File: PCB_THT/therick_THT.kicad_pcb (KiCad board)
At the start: 2 copper layers, 227 x 76.9 mm, 107 parts, among them J1 TYPE-C-31-M12_13, J2 4PIN, K1 KEYSW, K10 KEYSW, K11 KEYSW, K12 KEYSW, K13 KEYSW, K14 KEYSW, K15 KEYSW, K16 KEYSW, K17 KEYSW, K18 KEYSW, K19 KEYSW, K2 KEYSW, K20 KEYSW, K21 KEYSW, K22 KEYSW, K23 KEYSW, K24 KEYSW, K25 KEYSW, K26 KEYSW, K27 KEYSW, K28 KEYSW, K29 KEYSW, K3 KEYSW, K30 KEYSW, K31 KEYSW, K32 KEYSW, K33 KEYSW, K34 KEYSW, K35 KEYSW, K36 KEYSW, K37 KEYSW, K38 KEYSW, K39 KEYSW, K4 KEYSW, K40 KEYSW, K41 KEYSW, K42 KEYSW, K43 KEYSW, K44 KEYSW, K45 KEYSW, K46 KEYSW, K47 KEYSW, K48 KEYSW, K5 KEYSW, K6 KEYSW, K7 KEYSW, K8 KEYSW, K9 KEYSW, SW1 SW_PUSH, U1 ProMicro, U2 HOLE

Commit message: Slimmed down USB port
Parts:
- J1: footprint acheron_Connectors:TYPE-C-31-M-12 -> random-keyboard-parts:TYPE-C-31-M-12
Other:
- board size 227 x 76.9 mm -> 227 x 76.7 mm
- board text removed: "TYPE-C-31-M12"
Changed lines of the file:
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@@
   (general
     (thickness 1.6)
-    (drawings 36)
+    (drawings 35)
     (tracks 289)
     (zones 0)
@@
     (38 B.Mask user)
     (39 F.Mask user)
-    (40 Dwgs.User user)
+    (40 Dwgs.User user hide)
     (41 Cmts.User user)
     (42 Eco1.User user)
@@
     (46 B.CrtYd user)
     (47 F.CrtYd user)
-    (48 B.Fab user)
+    (48 B.Fab user hide)
     (49 F.Fab user)
   )
@@
     (uvia_min_size 0.2)
     (uvia_min_drill 0.1)
-    (edge_width 0.15)
+    (edge_width 0.05)
     (segment_width 0.15)
     (pcb_text_width 0.3)
@@
     (aux_axis_origin 160.3375 73.025)
     (grid_origin 160.3375 73.025)
-    (visible_elements 7FFFEFFF)
+    (visible_elements 7FFFFFFF)
     (pcbplotparams
       (layerselection 0x010fc_ffffffff)
@@
       (drillshape 0)
       (scaleselection 1)
-      (outputdirectory "../Gerber/"))
+      (outputdirectory "Gerber/"))
   )
   (net 0 "")
@@
     (uvia_drill 0.2)
   )
-  (module acheron_Connectors:TYPE-C-31-M-12 (layer B.Cu)
+  (module random-keyboard-parts:TYPE-C-31-M-12 (layer B.Cu)
     (at 84.1375 40.408625)
-    (fp_text reference J1 (at 0 -5) (layer B.SilkS)
-      (effects (font (size 1 1) (thickness 0.15)) (justify mirror))
+    (fp_text reference J1 (at -0.0127 -2.7305 180) (layer Dwgs.User)
+      (effects (font (size 1 1) (thickness 0.15)))
     )
-    (fp_text value TYPE-C-31-M12_13 (at 0.05 -7.35) (layer B.Fab)
+    (fp_text value TYPE-C-31-M12_13 (at 0.05 -7.35 180) (layer B.Fab)
       (effects (font (size 0.5 0.5) (thickness 0.125)) (justify mirror))
     )
-    (fp_line (start 4.8 -8.42) (end -4.8 -8.42) (layer Cmts.User) (width 0.15))
-    (fp_text user "KEEPOUT ZONE" (at 0 -4) (layer B.Fab)
+    (fp_line (start 5 -1.4) (end -5 -1.4) (layer Dwgs.User) (width 0.12))
+    (fp_line (start 5 -6.8) (end 5 -1.4) (layer Dwgs.User) (width 0.12))
+    (fp_line (start -5 -6.8) (end 5 -6.8) (layer Dwgs.User) (width 0.12))
+    (fp_line (start -5 -1.4) (end -5 -6.8) (layer Dwgs.User) (width 0.12))
+    (fp_text user "USB Connector" (at -0.0254 -4.7498) (layer B.SilkS)
+      (effects (font (size 0.5 0.5) (thickness 0.125)) (justify mirror))
+    )
+    (fp_text user TYPE-C-M-12 (at -0.0127 -4.0132) (layer B.SilkS)
       (effects (font (size 0.5 0.5) (thickness 0.125)) (justify mirror))
     )
+    (fp_line (start 4.8 -8.42) (end -4.8 -8.42) (layer Cmts.User) (width 0.15))
     (fp_line (start -5 -1.4) (end -5 -6.8) (layer B.Fab) (width 0.12))
     (fp_line (start -5 -6.8) (end 5 -6.8) (layer B.Fab) (width 0.12))
     (fp_line (start 5 -6.8) (end 5 -1.4) (layer B.Fab) (width 0.12))
     (fp_line (start 5 -1.4) (end -5 -1.4) (layer B.Fab) (width 0.12))
-    (fp_line (start -5 -5.5) (end -0.9 -1.4) (layer B.Fab) (width 0.05))
-    (fp_line (start -5 -4.5) (end -1.9 -1.4) (layer B.Fab) (width 0.05))
-    (fp_line (start -4.3 -6.8) (end -1.9 -4.5) (layer B.Fab) (width 0.05))
-    (fp_line (start -5 -3.5) (end -2.9 -1.4) (layer B.Fab) (width 0.05))
-    (fp_line (start -5 -2.5) (end -3.9 -1.4) (layer B.Fab) (width 0.05))
-    (fp_line (start -0.9 -3.4) (end 1.1 -1.4) (layer B.Fab) (width 0.05))
-    (fp_line (start -1.9 -3.4) (end 0.1 -1.4) (layer B.Fab) (width 0.05))
-    (fp_line (start -5 -6.5) (end -2.9 -4.5) (layer B.Fab) (width 0.05))
-    (fp_line (start -3.3 -6.8) (end -0.9 -4.5) (layer B.Fab) (width 0.05))
-    (fp_line (start 0.1 -3.4) (end 2.1 -1.4) (layer B.Fab) (width 0.05))
-    (fp_line (start 1.1 -3.4) (end 3.1 -1.4) (layer B.Fab) (width 0.05))
-    (fp_line (start -2.3 -6.8) (end 0.1 -4.5) (layer B.Fab) (width 0.05))
-    (fp_line (start -1.3 -6.8) (end 1.1 -4.5) (layer B.Fab) (width 0.05))
-    (fp_line (start 2.1 -3.4) (end 4.1 -1.4) (layer B.Fab) (width 0.05))
-    (fp_line (start 3.1 -3.4) (end 5 -1.5) (layer B.Fab) (width 0.05))
-    (fp_line (start -0.3 -6.8) (end 2.1 -4.5) (layer B.Fab) (width 0.05))
-    (fp_line (start 0.7 -6.8) (end 5 -2.5) (layer B.Fab) (width 0.05))
-    (fp_line (start 1.7 -6.8) (end 5 -3.5) (layer B.Fab) (width 0.05))
-    (fp_line (start 2.7 -6.8) (end 5 -4.5) (layer B.Fab) (width 0.05))
-    (fp_line (start 3.7 -6.8) (end 5 -5.5) (layer B.Fab) (width 0.05))
     (pad B4 smd roundrect (at 2.45 -1.275) (size 0.6 1.45) (drill (offset 0 0.55)) (layers B.Cu B.Paste B.Mask) (roundrect_rratio 0.25)
       (net 69 VCC))
@@
     (pad A4 smd roundrect (at -2.45 -1.275) (size 0.6 1.45) (drill (offset 0 0.55)) (layers B.Cu B.Paste B.Mask) (roundrect_rratio 0.25)
       (net 69 VCC))
-    (pad S thru_hole oval (at -4.3 -1.5) (size 1.016 2.159) (drill oval 0.6 1.7) (layers *.Cu *.Mask)
+    (pad S thru_hole oval (at -4.3 -1.5) (size 1.3 2.4) (drill oval 0.6 1.7) (layers *.Cu B.Mask)
       (net 66 GND))
     (pad A7 smd roundrect (at 0.25 -1.275) (size 0.3 1.45) (drill (offset 0 0.55)) (layers B.Cu B.Paste B.Mask) (roundrect_rratio 0.25)
@@
     (pad S thru_hole oval (at 4.3 -5.7) (size 1.3 1.9) (drill oval 0.6 1.2) (layers *.Cu *.Mask)
       (net 66 GND))
-    (pad S thru_hole oval (at 4.3 -1.5) (size 1.016 2.159) (drill oval 0.6 1.7) (layers *.Cu *.Mask)
+    (pad S thru_hole oval (at 4.3 -1.5) (size 1.3 2.4) (drill oval 0.6 1.7) (layers *.Cu *.Mask)
+      (net 66 GND))
+    (pad S smd oval (at -4.3 -1.5) (size 1.3 2.4) (layers F.Cu F.Mask)
       (net 66 GND))
     (model ":Acheron 3D models:TYPE-C-31-M-12.step"
@@
       (xy 4.278634 17.019493) (xy 5.507929 17.060663) (xy 6.737225 17.101833) (xy 7.015348 16.828876)) (layer B.SilkS) (width 0.01))
   )
-  (gr_text TYPE-C-31-M12 (at 84.1375 36.77725) (layer B.SilkS)
-    (effects (font (size 0.5 0.5) (thickness 0.125)) (justify mirror))
-  )
+  (gr_arc (start 79.862183 34.435) (end 79.862183 33.584942) (angle -90) (layer Edge.Cuts) (width 0.05))
+  (gr_arc (start 88.412817 34.435) (end 89.262875 34.435) (angle -90) (layer Edge.Cuts) (width 0.05))
   (dimension 5.334 (width 0.15) (layer Dwgs.User)
     (gr_text "5.334 mm" (at 40.593375 37.592 270) (layer Dwgs.User)
@@
   (gr_arc (start 178.990625 35.321875) (end 179.3875 35.321875) (angle -90) (layer Edge.Cuts) (width 0.05))
   (gr_arc (start 179.784375 35.321875) (end 179.3875 35.321875) (angle -90) (layer Edge.Cuts) (width 0.05))
-  (gr_arc (start 90.136625 34.925) (end 89.342875 34.925) (angle -90) (layer Edge.Cuts) (width 0.05))
-  (gr_arc (start 88.549125 34.242375) (end 89.342875 34.242375) (angle -90) (layer Edge.Cuts) (width 0.05))
-  (gr_arc (start 79.725875 34.242375) (end 79.725875 33.448625) (angle -90) (layer Edge.Cuts) (width 0.05))
-  (gr_arc (start 78.138375 34.925) (end 78.138375 35.71875) (angle -90) (layer Edge.Cuts) (width 0.05))
-  (gr_line (start 78.932125 34.242375) (end 78.932125 34.925) (layer Edge.Cuts) (width 0.05))
-  (gr_line (start 88.549125 33.448625) (end 79.725875 33.448625) (layer Edge.Cuts) (width 0.05))
-  (gr_line (start 89.342875 34.925) (end 89.342875 34.242375) (layer Edge.Cuts) (width 0.05))
-  (gr_line (start 144.859375 35.71875) (end 90.136625 35.71875) (layer Edge.Cuts) (width 0.05))
+  (gr_arc (start 90.056625 34.925) (end 89.262875 34.925) (angle -90) (layer Edge.Cuts) (width 0.05))
+  (gr_arc (start 78.218375 34.925) (end 78.218375 35.71875) (angle -90) (layer Edge.Cuts) (width 0.05))
+  (gr_line (start 79.012125 34.435) (end 79.012125 34.925) (layer Edge.Cuts) (width 0.05))
+  (gr_line (start 88.412817 33.584942) (end 79.862183 33.584942) (layer Edge.Cuts) (width 0.05))
+  (gr_line (start 89.262875 34.925) (end 89.262875 34.435) (layer Edge.Cuts) (width 0.05))
+  (gr_line (start 144.859375 35.71875) (end 90.056625 35.71875) (layer Edge.Cuts) (width 0.05))
   (gr_line (start 178.990625 34.925) (end 145.653125 34.925) (layer Edge.Cuts) (width 0.05))
   (gr_line (start 271.859375 35.71875) (end 179.784375 35.71875) (layer Edge.Cuts) (width 0.05))
@@
   (gr_line (start 48.815625 110.33125) (end 271.859375 110.33125) (layer Edge.Cuts) (width 0.05))
   (gr_line (start 46.83125 37.703125) (end 46.83125 108.346875) (layer Edge.Cuts) (width 0.05))
-  (gr_line (start 78.138375 35.71875) (end 48.815625 35.71875) (layer Edge.Cuts) (width 0.05))
+  (gr_line (start 78.218375 35.71875) (end 48.815625 35.71875) (layer Edge.Cuts) (width 0.05))
   (segment (start 256.78136 41.48125) (end 181.02155 41.48125) (width 0.25) (layer F.Cu) (net 1))
   (segment (start 63.89768 41.48176) (end 66.27896 41.48176) (width 0.25) (layer F.Cu) (net 1))

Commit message: Add image
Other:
- board text added: "therick_tht"
- board text removed: "therick"
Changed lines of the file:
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@@
   (gr_line (start 144.2085 48.006) (end 149.2885 48.006) (layer F.SilkS) (width 0.15))
   (gr_line (start 144.2085 40.64) (end 144.2085 48.006) (layer F.SilkS) (width 0.15))
-  (gr_text therick (at 215.1375 108.925) (layer B.SilkS)
-    (effects (font (size 2 2) (thickness 0.25)) (justify mirror))
+  (gr_text therick_tht (at 219.86875 108.925) (layer B.SilkS)
+    (effects (font (size 2 2) (thickness 0.25)) (justify left mirror))
   )
   (gr_arc (start 271.859375 37.703125) (end 273.84375 37.703125) (angle -90) (layer Edge.Cuts) (width 0.05))

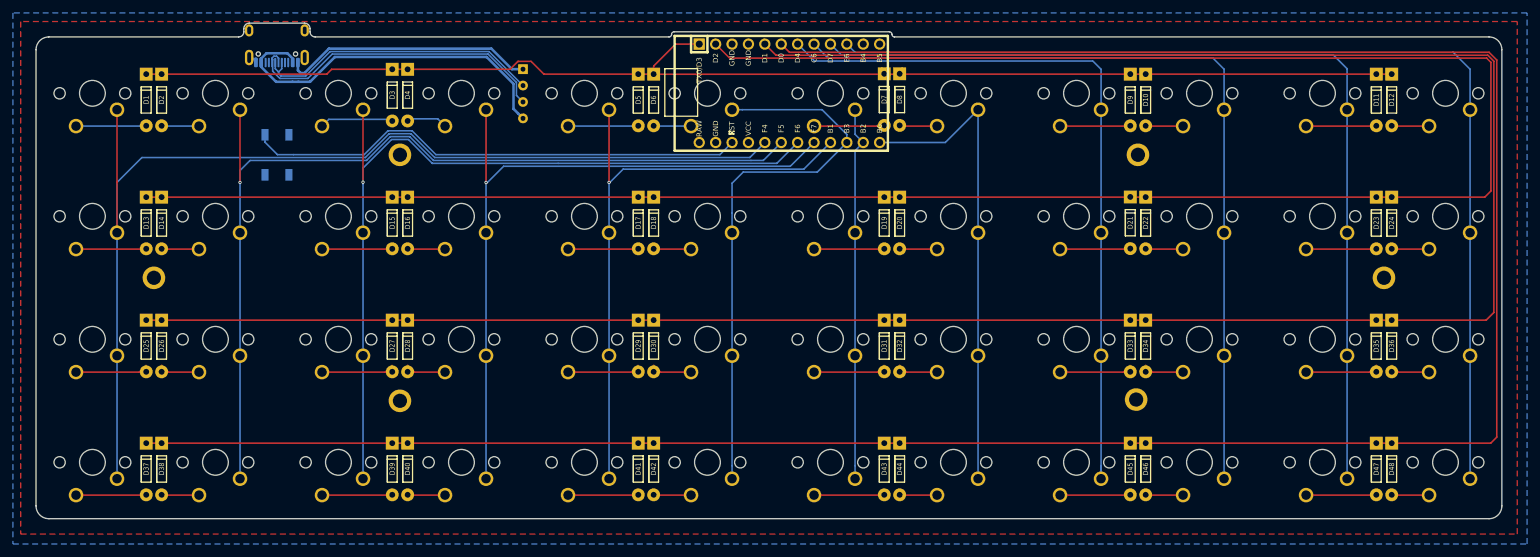
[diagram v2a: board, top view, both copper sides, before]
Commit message: Removed Type C Connector
Only uses a Pro Micro/Elite C now
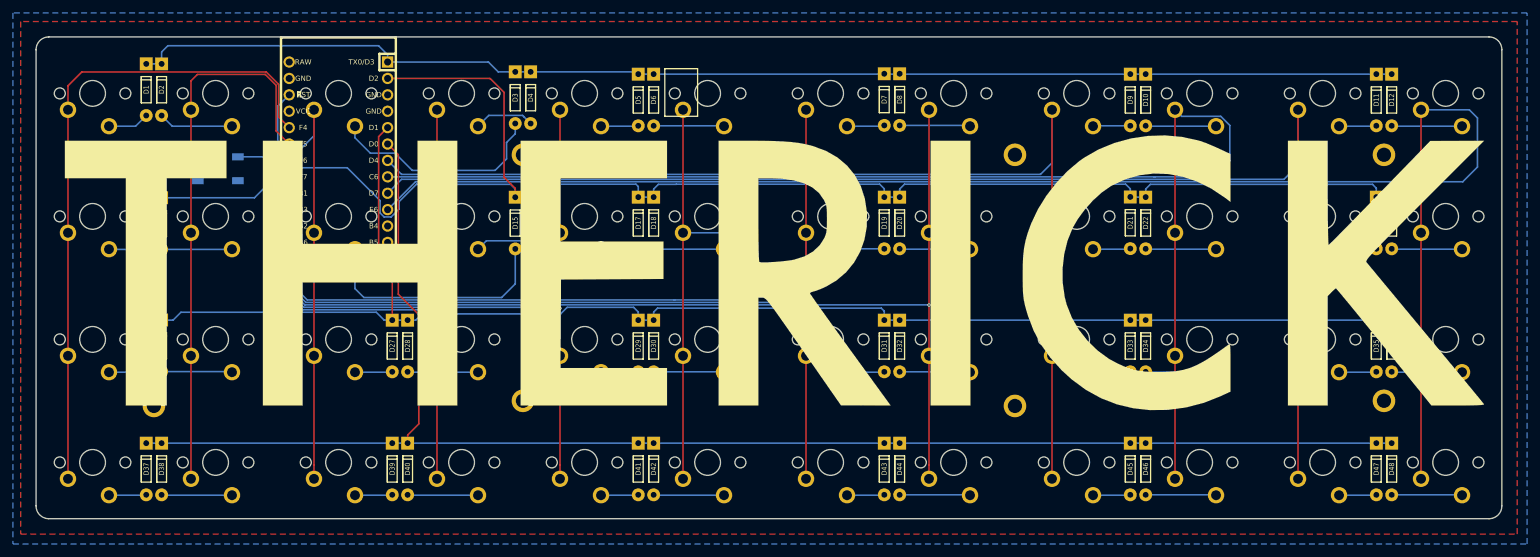
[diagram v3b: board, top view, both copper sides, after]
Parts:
- removed J1: TYPE-C-31-M12_13, random-keyboard-parts:TYPE-C-31-M-12
- removed J2: 4PIN, acheron_Connectors:PinHeader_1x4_P2.54mm_Vertical_B_mask
- added H7: MountingHole, random-keyboard-parts:Generic-Mounthole, F.Cu at (65.1, 54.0)
- added H8: MountingHole, random-keyboard-parts:Generic-Mounthole, F.Cu at (255.6, 92.1)
- added U3: HOLE, Artwork:THERICK, F.Cu at (160.3, 73.0)
- K1, K10, K11, K12, K13, K14, K15, K16, K17, K18, K19, K2, K20, K21, K22, K23, K24, K25, K26, K27, K28, K29, K3, K30, K31, K32, K33, K34, K35, K36, K37, K38, K39, K4, K40, K41, K42, K43, K44, K45, K46, K47, K48, K5, K6, K7, K8, K9: footprint MX_Only:MXOnly-1U-NoLED -> Keeb_footprints:MX100; moved to B.Cu
- moved U1 70.4 mm to (93.7, 53.6), turned to 270 degrees
- moved H1 19.8 mm to (65.1, 92.9)
- moved D3 19.1 mm to (121.0, 45.1)
- moved D4 19.1 mm to (123.4, 45.1)
- moved D15 19.1 mm to (121.0, 64.5)
- moved D16 19.1 mm to (123.4, 64.5)
- moved H4 19.1 mm to (198.4, 54.0)
- moved H6 19.1 mm to (255.6, 54.0)
- moved H2 19.0 mm to (122.2, 54.0)
- moved H3 19.0 mm to (122.2, 92.1)
- moved H5 18.8 mm to (198.4, 92.9)
- moved SW1 9.40 mm to (75.0, 56.1), turned to 180 degrees
- moved D1 1.59 mm to (63.9, 43.9)
- moved D2 1.59 mm to (66.3, 43.9)
- moved D14 0.10 mm to (66.3, 64.6)
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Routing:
- net /row3: track 379.8 -> 241.9 mm
- net /row2: track 362.1 -> 230.7 mm
- net /col6: track 58.2 -> 157.2 mm
- net /row1: track 349.8 -> 252.1 mm
- net /col7: track 74.5 -> 164.5 mm, vias 0 -> 1
- net /col11: track 161.6 -> 245.5 mm
- net /col9: track 128.5 -> 203.7 mm
- net /col5: track 86.8 -> 156.5 mm
- net /col0: track 170.9 -> 102.6 mm
- net /col2: track 131.7 -> 66.6 mm, vias 1 -> 0
- net /col10: track 145.1 -> 208.5 mm
- net Net-(SW1-Pad2): track 78.1 -> 15.7 mm
- net /col1: track 147.7 -> 85.9 mm, vias 1 -> 0
- net VCC: track 56.2 -> 0.00 mm
- net /col8: track 114.0 -> 169.9 mm
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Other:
- board size 227 x 76.7 mm -> 227 x 74.6 mm
- board text added: "PCB Rev 1.1"
